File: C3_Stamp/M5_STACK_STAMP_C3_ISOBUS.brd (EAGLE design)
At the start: 20.3 x 22.9 mm, 3 parts, among them J1 61300811121, J2 61300611121

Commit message: ..
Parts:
- added C1, C2, C4, C5: FG18X7R1H104KNT06, FG18X7R1H104KNT06-pcb-part-libraries:FG18C0G1H101JNT06
- added C3: FG28X7R1H473KNT06, FG28X7R1H473KNT06-pcb-part-libraries:FG28
- added IC1: MCP2562-E_P, MCP2562-E_P-pcb-part-libraries:DIP781W56P254L950H533Q8N
- added J3: DTF13-4P, DTF13-4P-pcb-part-libraries:DTF134P
- added R1, R2: (no value), resistor:0204/7
- added U1: (no value), Wurth_Step Down Converter_MagI³C-FDSM:MAGI³C-FDSM_173XXXX42
- moved J1 11.5 mm to (2.54, 11.4)
- moved J2 11.5 mm to (20.3, 8.89)
- moved U$1 11.5 mm to (2.54, 20.3)
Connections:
- new net +12V: C4.2, J3.1, U1.1
- new net +3V3: C2.2, IC1.5, J2.6
- new net +5V: C1.2, C5.2, IC1.3, J1.8, U1.3
- new net CAN_N: IC1.6, J3.4, R2.1
- new net CAN_P: IC1.7, J3.2, R1.2
- new net EN: J2.3
- new net G10: J1.7
- new net G20: IC1.4, J2.4
- new net G21: IC1.1, J2.5
- new net G4: J1.2
- new net G5: J1.3
- new net G6: J1.4
- new net G7: J1.5
- new net G8: J1.6
- new net G9: J2.2
- new net GND: C1.1, C2.1, C3.2, C4.1, C5.1, IC1.2, IC1.8, J1.1, J2.1, J3.3, U1.2
- new net N$1: C3.1, R1.1, R2.2
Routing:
- added copper zone on layer 1, net GND
- added copper zone on layer 16, net GND
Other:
- board size 20.3 x 22.9 mm -> 52.1 x 29.2 mm

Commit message: Order !
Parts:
- moved C3 5.08 mm to (38.1, 20.3)
- moved U1 2.54 mm to (27.9, 25.4)
- moved R2 2.54 mm to (35.6, 14.0)
- moved R1 2.54 mm to (40.6, 16.5), turned to 270 degrees
- turned C4 to 270 degrees
- turned C5 to 270 degrees
- turned J1 to 270 degrees
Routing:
- net +5V: track 0.00 -> 60.9 mm
- net CAN_P: track 0.00 -> 21.9 mm
- net +3V3: track 0.00 -> 20.9 mm
- net +12V: track 0.00 -> 18.6 mm
- net CAN_N: track 0.00 -> 14.4 mm
- net G21: track 0.00 -> 6.13 mm
- net G20: track 0.00 -> 6.13 mm
- net N$1: track 0.00 -> 6.13 mm
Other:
- board size 52.1 x 29.2 mm -> 53.3 x 30.5 mm

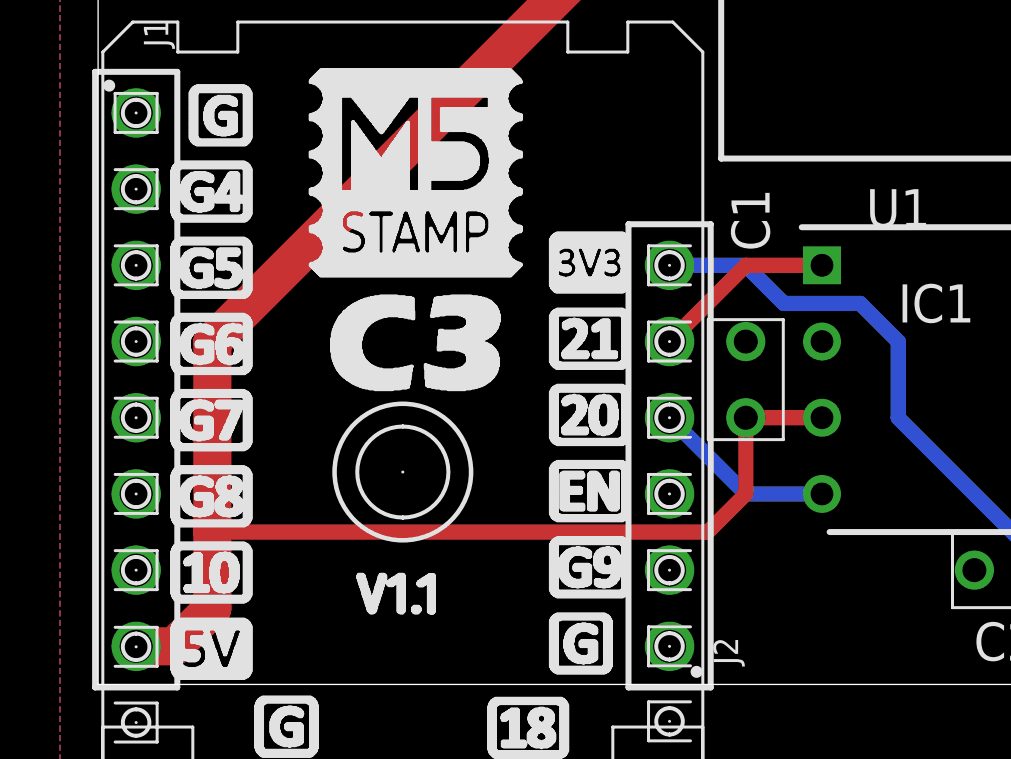
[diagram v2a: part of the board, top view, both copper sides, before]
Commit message: was a bad bug about 2 Pins.
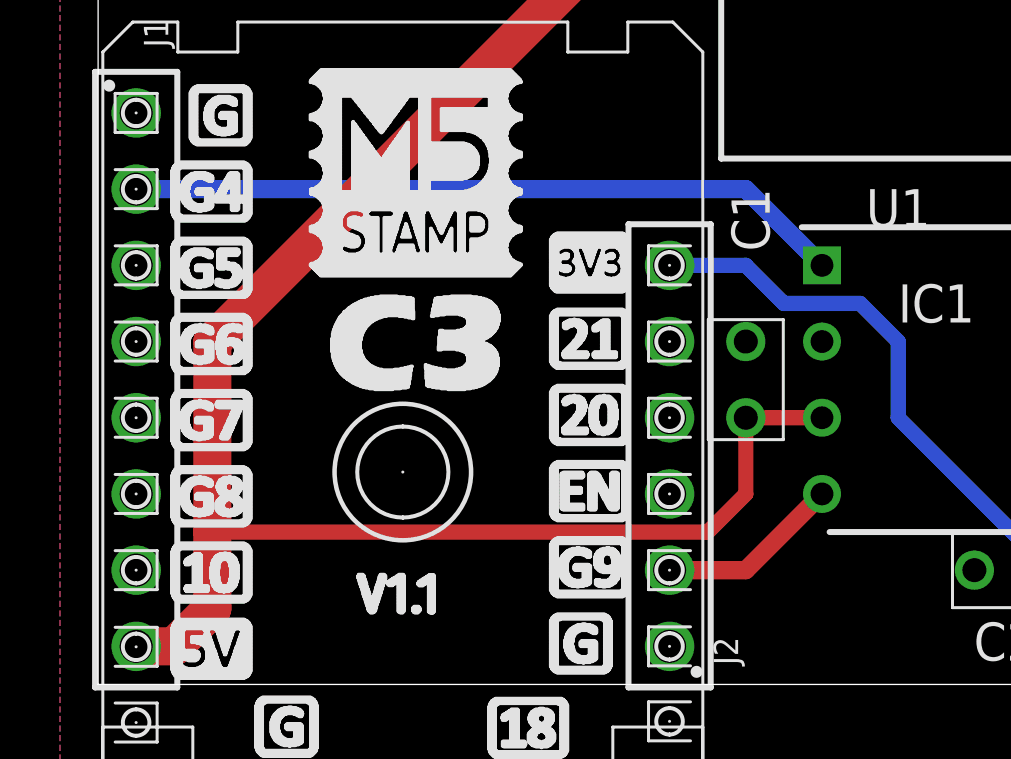
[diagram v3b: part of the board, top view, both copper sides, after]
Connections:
- net G20: no longer IC1.4
- net G21: no longer IC1.1
- net G4: now also IC1.1
- net G9: now also IC1.4
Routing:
- net G4: track 0.00 -> 23.9 mm
- net G9: track 0.00 -> 6.13 mm
- net G21: track 6.13 -> 0.00 mm
- net G20: track 6.13 -> 0.00 mm
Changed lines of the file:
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@@
 <signal name="G9">
 <contactref element="J2" pad="2"/>
+<contactref element="IC1" pad="4"/>
+<wire x1="20.32" y1="5.08" x2="22.86" y2="5.08" width="0.6096" layer="1"/>
+<wire x1="22.86" y1="5.08" x2="25.4" y2="7.62" width="0.6096" layer="1"/>
 </signal>
 <signal name="EN">
@@
 <signal name="G4">
 <contactref element="J1" pad="2"/>
+<contactref element="IC1" pad="1"/>
+<wire x1="25.4" y1="15.24" x2="22.86" y2="17.78" width="0.6096" layer="16"/>
+<wire x1="22.86" y1="17.78" x2="2.54" y2="17.78" width="0.6096" layer="16"/>
 </signal>
 <signal name="G21">
-<contactref element="IC1" pad="1"/>
 <contactref element="J2" pad="5"/>
-<wire x1="20.32" y1="12.7" x2="22.86" y2="15.24" width="0.508" layer="1"/>
-<wire x1="22.86" y1="15.24" x2="25.4" y2="15.24" width="0.508" layer="1"/>
 </signal>
 <signal name="G20">
-<contactref element="IC1" pad="4"/>
 <contactref element="J2" pad="4"/>
-<wire x1="20.32" y1="10.16" x2="22.86" y2="7.62" width="0.508" layer="16"/>
-<wire x1="22.86" y1="7.62" x2="25.4" y2="7.62" width="0.508" layer="16"/>
 </signal>
 </signals>
